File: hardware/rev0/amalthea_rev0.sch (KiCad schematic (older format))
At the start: 25 parts, among them J1 USB_B_Micro, J2 USB_B_Micro, J3 Conn_Coaxial, J4 Conn_Coaxial, J8 Conn_Coaxial, J9 Conn_Coaxial, SW1 BTN_RECOVERY, SW2 BTN_DFU, SW3 BTN_RESET, Y1 DSC60xx

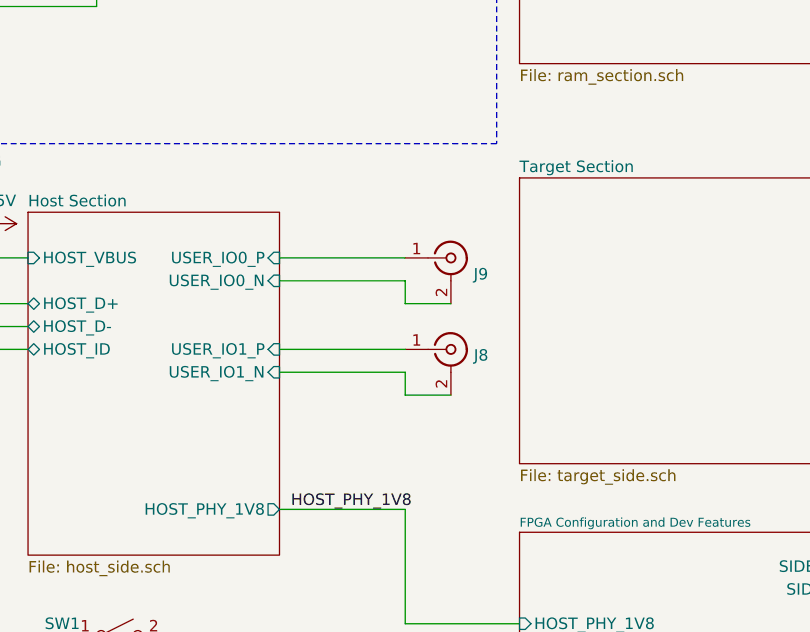
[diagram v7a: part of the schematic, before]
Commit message: Rejig user IO
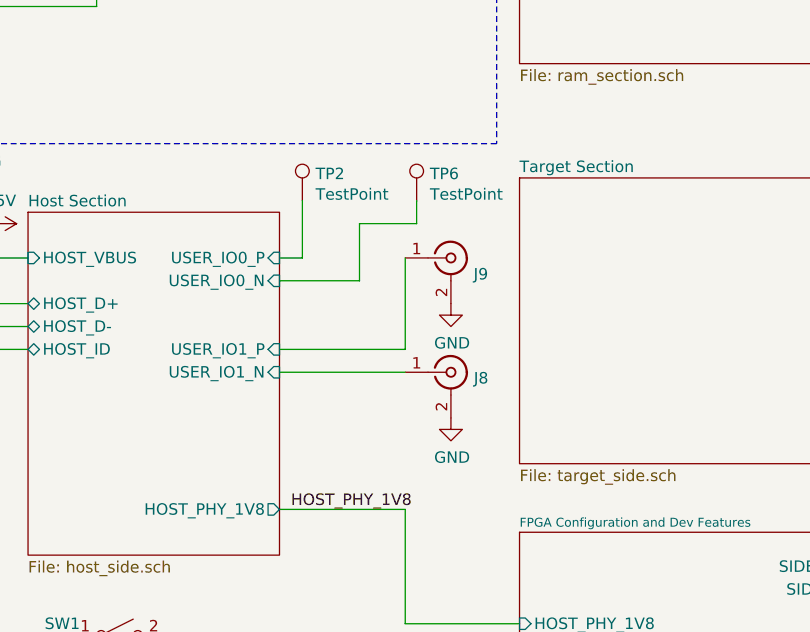
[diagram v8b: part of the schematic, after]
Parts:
- added TP2, TP6: TestPoint, TestPoint:TestPoint_Pad_D1.0mm, symbol Connector:TestPoint
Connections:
- net GND: now also J8.2 (Ext), J9.2 (Ext)
- net Host Section/USER_IO0_N: now also TP6.1; no longer J9.2 (Ext)
- net Host Section/USER_IO0_P: now also TP2.1; no longer J9.1 (In)
- net Host Section/USER_IO1_N: now also J8.1 (In); no longer J8.2 (Ext)
- net Host Section/USER_IO1_P: now also J9.1 (In); no longer J8.1 (In)
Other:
- moved on the sheet: J8
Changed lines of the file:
@@
 L Connector:Conn_Coaxial J8
 U 1 1 5E41D377
-P 3700 4100
-F 0 "J8" H 3800 4074 50  0000 L CNN
-F 1 "Conn_Coaxial" H 3800 3984 50  0001 L CNN
-F 2 "amalthea:SMA-EDGE" H 3700 4100 50  0001 C CNN
-F 3 " ~" H 3700 4100 50  0001 C CNN
-	1    3700 4100
+P 3700 4200
+F 0 "J8" H 3800 4174 50  0000 L CNN
+F 1 "Conn_Coaxial" H 3800 4084 50  0001 L CNN
+F 2 "amalthea:SMA-EDGE" H 3700 4200 50  0001 C CNN
+F 3 " ~" H 3700 4200 50  0001 C CNN
+	1    3700 4200
 	1    0    0    -1
 $EndComp
@@
 $EndComp
 Wire Wire Line
-	2950 3700 3500 3700
-Wire Wire Line
-	2950 3800 3500 3800
-Wire Wire Line
-	3500 3800 3500 3900
-Wire Wire Line
-	3500 3900 3700 3900
-Wire Wire Line
-	2950 4100 3500 4100
-Wire Wire Line
 	2950 4200 3500 4200
-Wire Wire Line
-	3500 4200 3500 4300
-Wire Wire Line
-	3500 4300 3700 4300
 $Comp
 L power:PWR_FLAG #FLG0101
@@
 Wire Wire Line
 	1550 3550 1700 3550
+$Comp
+L power:GND #PWR0142
+U 1 1 5EEEE881
+P 3700 4400
+F 0 "#PWR0142" H 3700 4150 50  0001 C CNN
+F 1 "GND" H 3705 4227 50  0000 C CNN
+F 2 "" H 3700 4400 50  0001 C CNN
+F 3 "" H 3700 4400 50  0001 C CNN
+	1    3700 4400
+	1    0    0    -1
+$EndComp
+$Comp
+L power:GND #PWR0143
+U 1 1 5EEF3D86
+P 3700 3900
+F 0 "#PWR0143" H 3700 3650 50  0001 C CNN
+F 1 "GND" H 3705 3727 50  0000 C CNN
+F 2 "" H 3700 3900 50  0001 C CNN
+F 3 "" H 3700 3900 50  0001 C CNN
+	1    3700 3900
+	1    0    0    -1
+$EndComp
+Wire Wire Line
+	2950 4100 3500 4100
+Wire Wire Line
+	3500 4100 3500 3700
+$Comp
+L Connector:TestPoint TP2
+U 1 1 5EEFB3F1
+P 3050 3450
+F 0 "TP2" H 3108 3568 50  0000 L CNN
+F 1 "TestPoint" H 3108 3478 50  0000 L CNN
+F 2 "TestPoint:TestPoint_Pad_D1.0mm" H 3250 3450 50  0001 C CNN
+F 3 "~" H 3250 3450 50  0001 C CNN
+	1    3050 3450
+	1    0    0    -1
+$EndComp
+$Comp
+L Connector:TestPoint TP6
+U 1 1 5EEFBF5B
+P 3550 3450
+F 0 "TP6" H 3608 3568 50  0000 L CNN
+F 1 "TestPoint" H 3608 3478 50  0000 L CNN
+F 2 "TestPoint:TestPoint_Pad_D1.0mm" H 3750 3450 50  0001 C CNN
+F 3 "~" H 3750 3450 50  0001 C CNN
+	1    3550 3450
+	1    0    0    -1
+$EndComp
+Wire Wire Line
+	3050 3450 3050 3700
+Wire Wire Line
+	3050 3700 2950 3700
+Wire Wire Line
+	2950 3800 3300 3800
+Wire Wire Line
+	3300 3800 3300 3550
+Wire Wire Line
+	3300 3550 3550 3550
+Wire Wire Line
+	3550 3550 3550 3450
 $EndSCHEMATC
